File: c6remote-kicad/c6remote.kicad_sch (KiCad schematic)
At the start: 38 parts, among them J1 Battery, Q1 MMBT2222A, Q2 AO3401A, Q3 AO3401A, SW1 SW_Push, SW10 SW_Push, SW11 SW_Push, SW2 SW_Push, SW3 SW_Push, SW4 SW_Push, SW5 SW_Push, SW6 SW_Push, SW7 SW_Push, SW8 SW_Push, SW9 SW_Push, U1 XIAO-ESP32-C6, U2 TSOP4136, U3 PCF8575DBR

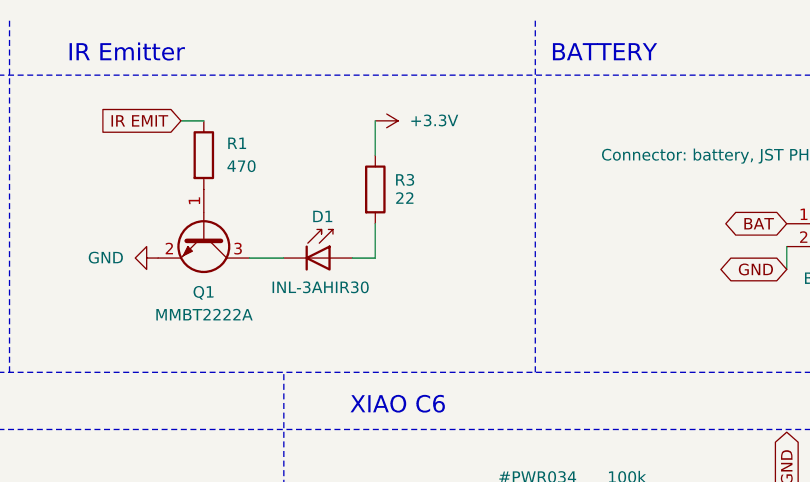
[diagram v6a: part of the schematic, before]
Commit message: feat(pcb): drop R3 from 22R to 10R and move D1 to the back face at 61.98,32.75, taking the IR emitter from about 70mA to 130-150mA so it stops loafing at 70% of its 100mA DC rating and 7% of its 1A pulse rating, which is roughly double the radiant intensity and 1.4x the range for one part value; R1 stays 470R, so 5.4mA of base gives a forced beta of 28 rather than the Ic/10 rule of thumb and Q1's Vce(sat) rather than the resistor sets where in that band it lands, dropping R1 to 220R for 11.6mA of base is the follow-up if the last 15% is wanted and is still inside the C6's GPIO limits; 150mA is above the INL-3AHIR30's 100mA DC rating but well inside its 1A pulse rating at 1/10 duty and 1kHz, which is the regime an IR burst actually runs in, and R3's 0.225W instantaneous against a 0.1W 0603 is a few mW averaged over a frame; sourcing follows the value with MPN RC0603FR-0722RL to RC0603FR-0710RL and both distributor links repointed, so the BOM's R3 row changes but the line count does not; D1 moving to B.Cu is what a top-edge emitter wants now that the body hangs under the board with the leads still bent into the notch, and it left no dangling copper; ERC 0, DRC 1 warning (the inherited U1 lib_footprint_mismatch), 0 unconnected and parity 0, zones refilled in the GUI and the stored fill reproduces under --refill-zones; silk stays 2026.8.1, which is still what the next push to main computes since 2026.8.0 is the newest tag
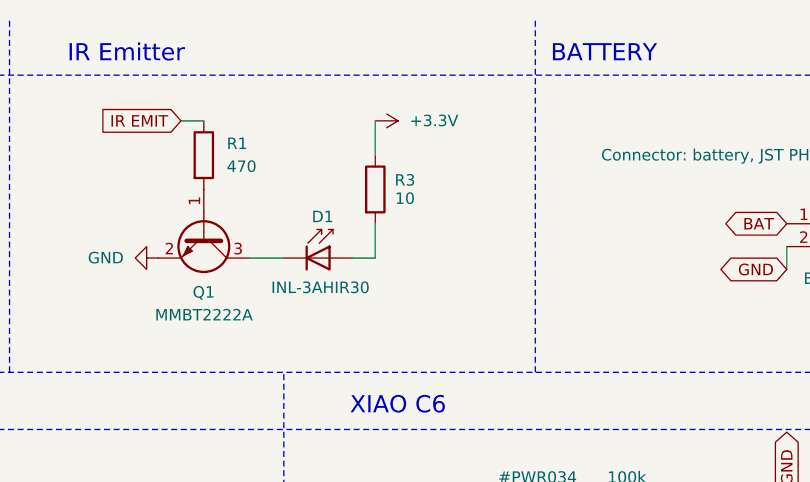
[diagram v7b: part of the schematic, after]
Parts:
- R3: value 22 -> 10; Digikey https://www.digikey.com/en/products/detail/yageo/RC0603FR-0722RL/727055 -> https://www.digikey.com/en/products/detail/yageo/RC0603FR-0710RL/726879; MPN RC0603FR-0722RL -> RC0603FR-0710RL; Mouser https://www.mouser.com/ProductDetail/YAGEO/RC0603FR-0722RL -> https://www.mouser.com/ProductDetail/YAGEO/RC0603FR-0710RL
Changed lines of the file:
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@@
 			)
 		)
-		(property "Value" "22"
+		(property "Value" "10"
 			(at 169.672 31.496 0)
 			(show_name no)
@@
 			)
 		)
-		(property "Description" "Resistor: 22R 1% 0.1W 0603 (D1 IR LED current limit)"
+		(property "Description" "Resistor: 10R 1% 0.1W 0603 (D1 IR LED current limit)"
 			(at 166.37 30.48 0)
 			(hide yes)
@@
 			)
 		)
-		(property "Digikey" "https://www.digikey.com/en/products/detail/yageo/RC0603FR-0722RL/727055"
+		(property "Digikey" "https://www.digikey.com/en/products/detail/yageo/RC0603FR-0710RL/726879"
 			(at 0 0 0)
 			(hide yes)
@@
 			)
 		)
-		(property "Mouser" "https://www.mouser.com/ProductDetail/YAGEO/RC0603FR-0722RL"
+		(property "Mouser" "https://www.mouser.com/ProductDetail/YAGEO/RC0603FR-0710RL"
 			(at 0 0 0)
 			(hide yes)
@@
 			)
 		)
-		(property "MPN" "RC0603FR-0722RL"
+		(property "MPN" "RC0603FR-0710RL"
 			(at 0 0 0)
 			(hide yes)

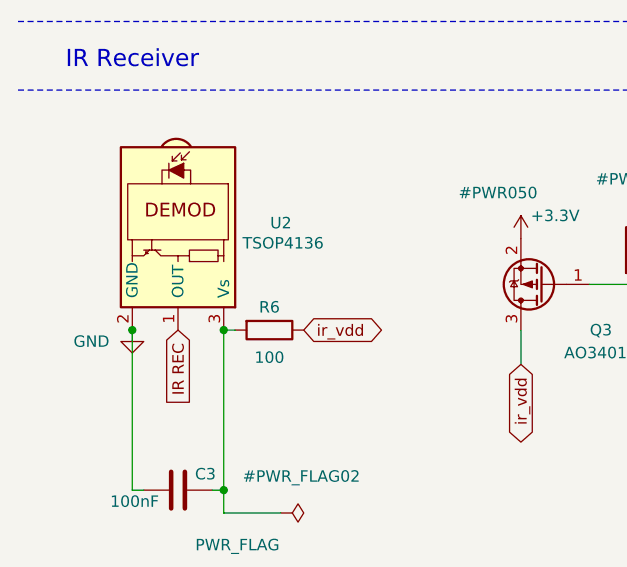
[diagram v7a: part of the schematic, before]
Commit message: feat(pcb): swap U2 from the through-hole TSOP4136 to the SMD TSOP6136 on a new Library:Vishay_PANHEAD-4Pin_SideView footprint at 42.845,31.8575 on B.Cu, which keeps the AGC1 setting so the set of remote codes the receiver will decode is unchanged and takes the tallest bottom-side keepout from 10.43mm down to 5.34mm; ROADMAP's TSOP75336 candidate is rejected rather than adopted because Vishay's Heimdall package carries no AGC1 part at all and AGC3 buys noise suppression by narrowing code acceptance, which is the wrong trade for a receiver both firmwares run with dump: all against arbitrary remotes, and the height difference between the two SMD candidates, 5.3mm against 3.0mm, is immaterial next to the 10.43mm the through-hole part stood; pinning moves from 1 OUT, 2 GND, 3 Vs to 1 GND, 2 N.C., 3 Vs, 4 OUT, so the symbol is a new Local:TSOP61xx whose OUT, GND and Vs sit on the old pin coordinates and no wire endpoint moved, only the numbers, with a no-connect flag on pad 2 and a via off pad 1 into the F.Cu GND pour because B.Cu is the +3.3V plane and an SMD pad cannot reach it through a barrel the way the old through-hole pad did; land pattern is four 0.9 x 2.2 pads on 1.27 pitch per datasheet 82457 page 7, TT and TR are tape attitudes rather than two mounting orientations so there is one pattern, and the 3D model is Vishay doc 82826 pre-rotated on export so the footprint needs no offset or rotate; sourcing follows the part with MPN TSOP6136TT and both distributor links repointed, so the BOM's U2 row changes but the line count does not and the position file stays at 37 rows; ERC 0, DRC 1 warning (the inherited U1 lib_footprint_mismatch), 0 unconnected and parity 0, with all 171 board pad nets diffed against the schematic netlist for zero mismatches after the F8 sync, zones refilled in the GUI; silk stays 2026.8.1, which is still what the next push to main computes since 2026.8.0 is the newest tag
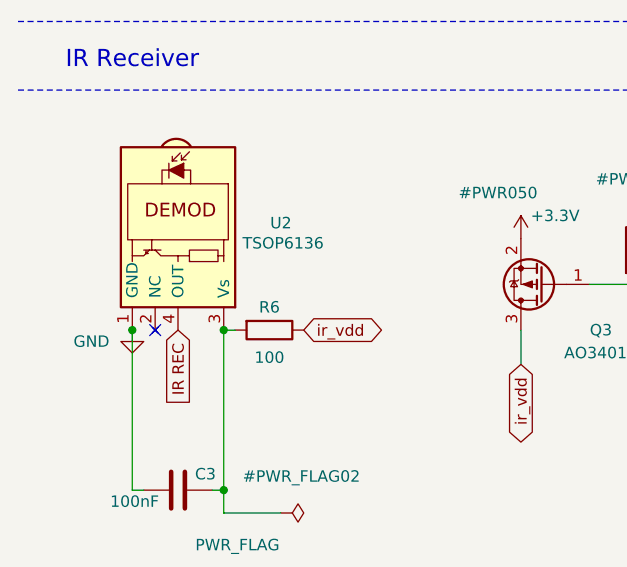
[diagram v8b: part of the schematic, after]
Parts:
- U2: value TSOP4136 -> TSOP6136; footprint OptoDevice:Vishay_MOLD-3Pin -> Library:Vishay_PANHEAD-4Pin_SideView; symbol Interface_Optical:TSOP45xx -> Local:TSOP61xx; Digikey https://www.digikey.com/en/products/detail/vishay-semiconductor-opto-division/TSOP4136/4074522 -> https://www.digikey.com/en/products/detail/vishay-semiconductor-opto-division/TSOP6136TT/4075852; MPN TSOP4136 -> TSOP6136TT; Mouser https://www.mouser.com/ProductDetail/Vishay-Semiconductors/TSOP4136 -> https://www.mouser.com/ProductDetail/Vishay-Semiconductors/TSOP6136TT
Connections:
- net GND: now also U2.1 (GND); no longer U2.2 (GND)
- net IR REC: now also U2.4 (OUT); no longer U2.1 (OUT)
- no-connect marks 5 -> 6
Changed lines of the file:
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@@
 	)
 	(no_connect
+		(at 26.67 163.83)
+	)
+	(no_connect
 		(at 223.52 68.58)
 	)
@@
 	)
 	(symbol
-		(lib_id "Interface_Optical:TSOP45xx")
+		(lib_id "Local:TSOP61xx")
 		(at 29.21 153.67 270)
 		(unit 1)
@@
 			)
 		)
-		(property "Value" "TSOP4136"
+		(property "Value" "TSOP6136"
 			(at 40.894 154.178 90)
 			(show_name no)
@@
 			)
 		)
-		(property "Footprint" "OptoDevice:Vishay_MOLD-3Pin"
+		(property "Footprint" "Library:Vishay_PANHEAD-4Pin_SideView"
 			(at 19.685 152.4 0)
 			(hide yes)
@@
 			)
 		)
-		(property "Datasheet" "http://www.vishay.com/docs/82460/tsop45.pdf"
+		(property "Datasheet" "https://www.vishay.com/docs/82457/tsop61.pdf"
 			(at 36.83 170.18 0)
 			(hide yes)
@@
 			)
 		)
-		(property "Digikey" "https://www.digikey.com/en/products/detail/vishay-semiconductor-opto-division/TSOP4136/4074522"
+		(property "Digikey" "https://www.digikey.com/en/products/detail/vishay-semiconductor-opto-division/TSOP6136TT/4075852"
 			(at 67.31 68.58 0)
 			(hide yes)
@@
 			)
 		)
-		(property "Mouser" "https://www.mouser.com/ProductDetail/Vishay-Semiconductors/TSOP4136"
+		(property "Mouser" "https://www.mouser.com/ProductDetail/Vishay-Semiconductors/TSOP6136TT"
 			(at 67.31 68.58 0)
 			(hide yes)
@@
 			)
 		)
-		(property "MPN" "TSOP4136"
+		(property "MPN" "TSOP6136TT"
 			(at 67.31 68.58 0)
 			(hide yes)
@@
 		(pin "1"
 		)
+		(pin "2"
+		)
 		(pin "3"
 		)
-		(pin "2"
+		(pin "4"
 		)
 		(instances
